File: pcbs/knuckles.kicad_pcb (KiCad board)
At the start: 2 copper layers, 137.3 x 113.5 mm, 152 parts

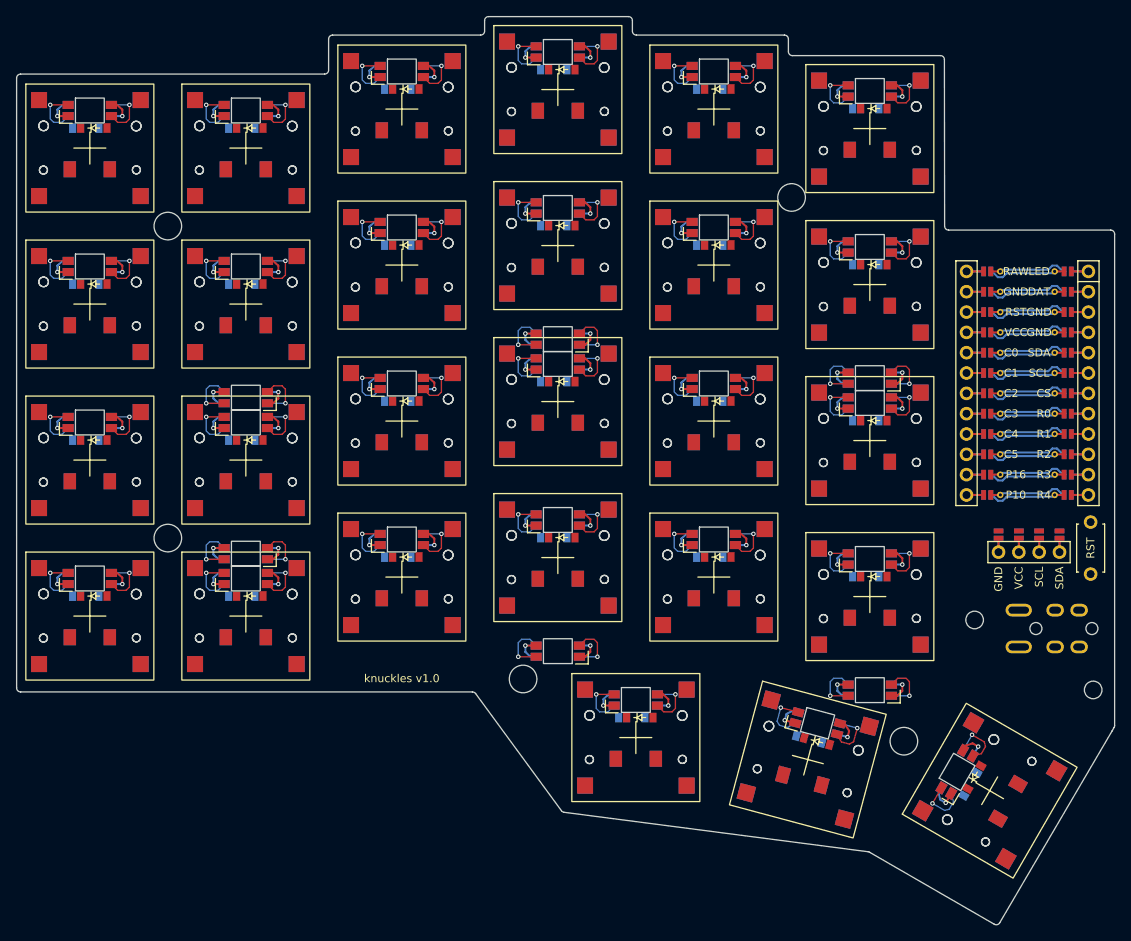
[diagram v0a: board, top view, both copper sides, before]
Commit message: feat: default to compact 18.5 mm layout and refresh generated boards
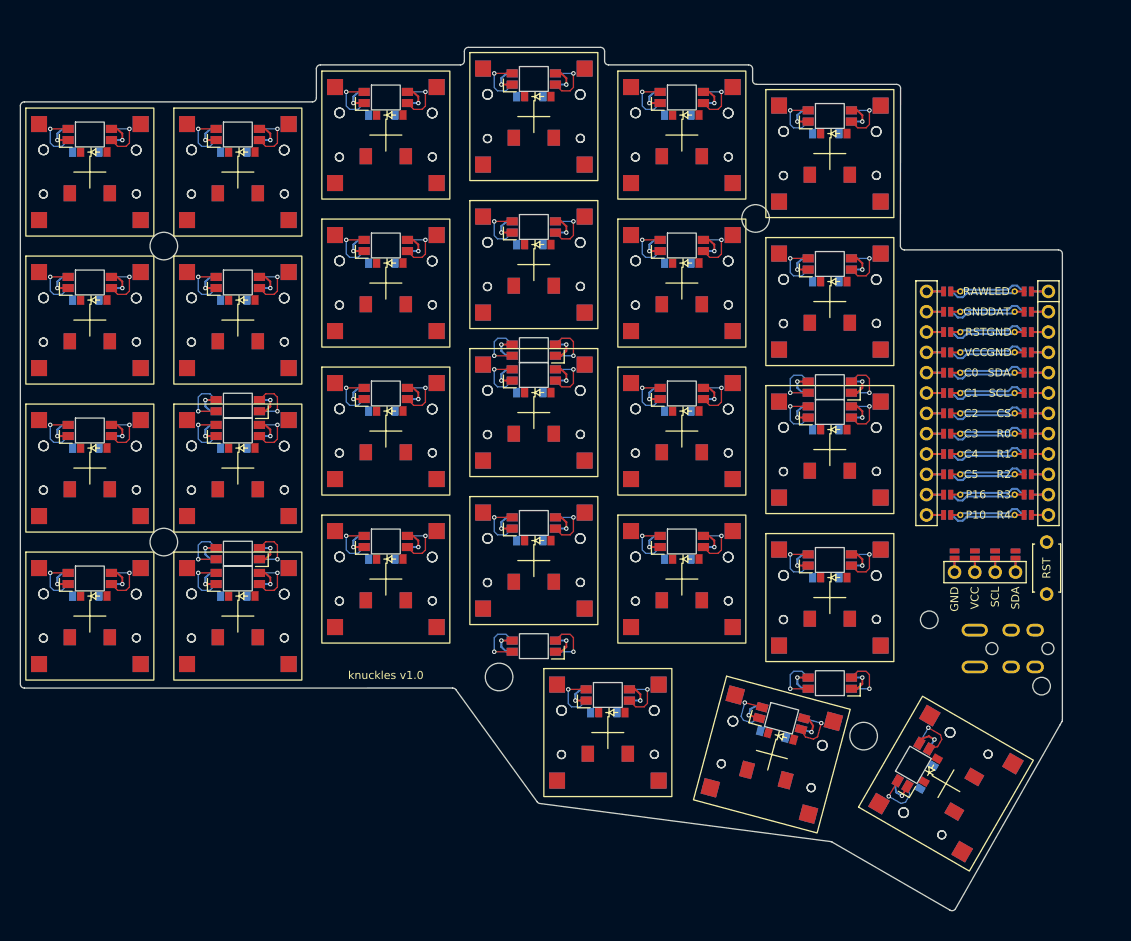
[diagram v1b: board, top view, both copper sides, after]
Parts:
- moved MH2 6.47 mm to (219.0, 108.8)
- moved DISP1 6.04 mm to (211.9, 77.8)
- moved RST1 6.04 mm to (219.6, 94.0)
- moved TRRS1 6.04 mm to (221.4, 104.1)
- moved D24 5.90 mm to (192.0, 39.7)
- moved D51 5.90 mm to (193.0, 39.7)
- moved LED24 5.90 mm to (192.5, 37.5)
- moved S24 5.90 mm to (192.5, 42.2)
- moved S51 5.90 mm to (192.5, 42.2)
- moved MH1 5.67 mm to (204.9, 100.5)
- moved MCU1 5.59 mm to (212.2, 72.1)
- moved D27 5.54 mm to (204.6, 120.1)
- moved D54 5.54 mm to (205.1, 119.3)
- moved LED27 5.54 mm to (202.9, 118.6)
- moved S27 5.54 mm to (207.0, 120.9)
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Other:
- board size 137.3 x 113.5 mm -> 130.3 x 107.9 mm
